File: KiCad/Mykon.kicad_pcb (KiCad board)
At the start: 2 copper layers, 68.4 x 55.4 mm, 27 parts, among them U1 MCP23017_SO, U2 ADS1115IDGS

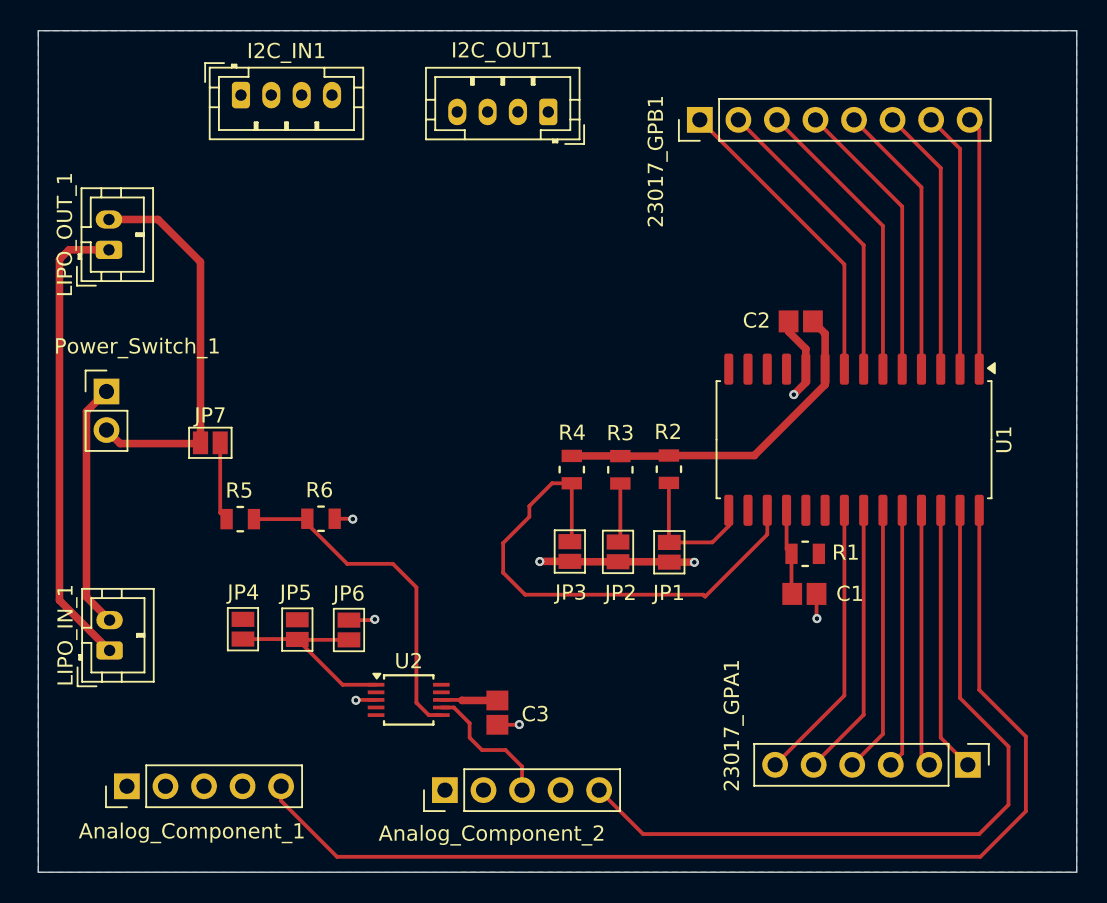
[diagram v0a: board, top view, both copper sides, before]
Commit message: Working ADS1115 and MCP23017
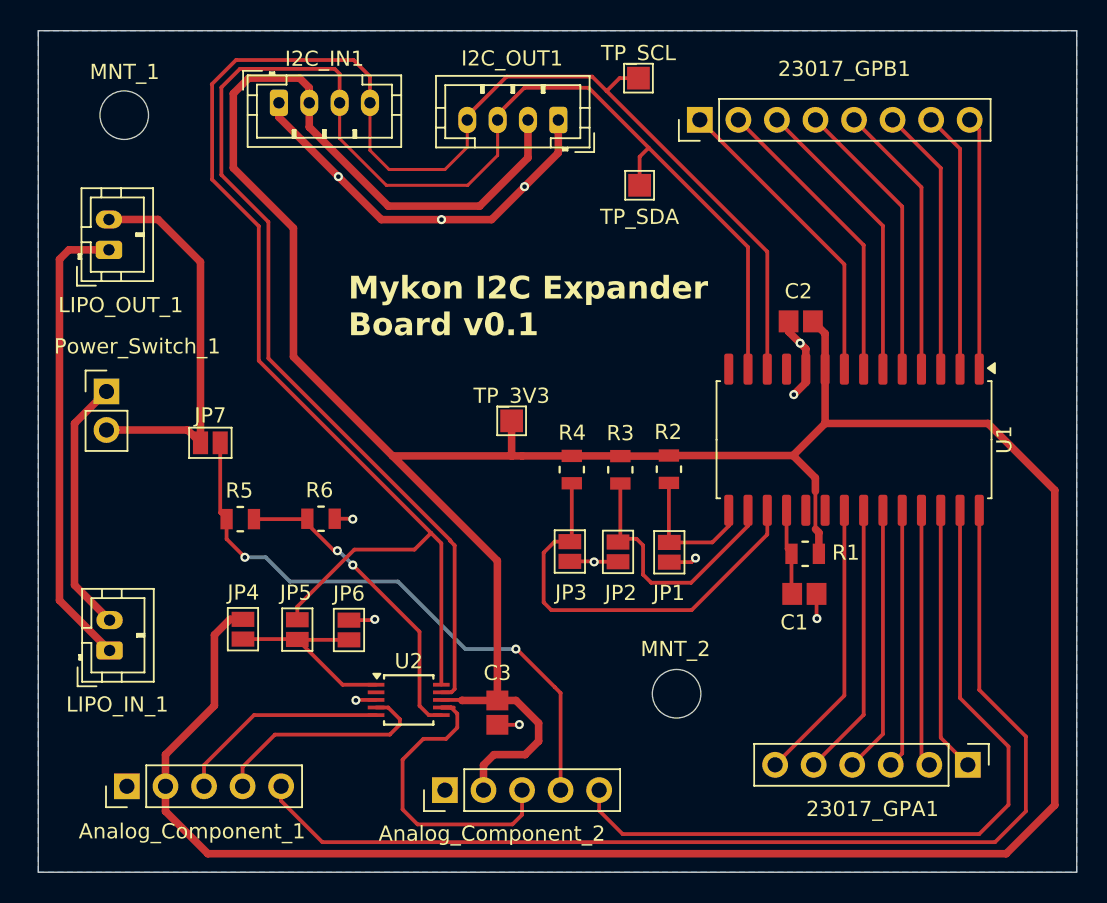
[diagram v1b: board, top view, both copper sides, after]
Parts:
- added MNT_1: MountingHole_3.2mm_M3, MountingHole:MountingHole_3.2mm_M3, F.Cu at (111.9, 77.2)
- added MNT_2: MountingHole_3.2mm_M3, MountingHole:MountingHole_3.2mm_M3, F.Cu at (148.3, 115.3)
- added TP_3V3: TestPoint_Pad_1.5x1.5mm, TestPoint:TestPoint_Pad_1.5x1.5mm, F.Cu at (137.4, 97.3)
- added TP_SCL: TestPoint_Pad_1.5x1.5mm, TestPoint:TestPoint_Pad_1.5x1.5mm, F.Cu at (145.8, 74.8)
- added TP_SDA: TestPoint_Pad_1.5x1.5mm, TestPoint:TestPoint_Pad_1.5x1.5mm, F.Cu at (145.9, 81.8)
- moved I2C_IN1 2.55 mm to (122.1, 76.4)
- moved I2C_OUT1 0.85 mm to (140.5, 77.5)
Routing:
- net +3V3: track 26.9 -> 250.0 mm
- net SCL: track 0.00 -> 119.3 mm
- net SDA: track 0.00 -> 107.2 mm
- net Net-(Analog_Component_2-Pin_4): track 5.20 -> 39.1 mm, vias 0 -> 2
- net GND: track 23.2 -> 44.2 mm, vias 8 -> 12
- net Net-(Analog_Component_1-Pin_4): track 0.00 -> 15.0 mm
- net Net-(Analog_Component_1-Pin_3): track 0.00 -> 14.1 mm
- net Net-(JP2-A): track 3.92 -> 17.0 mm
- net Net-(Analog_Component_2-Pin_3): track 9.04 -> 20.9 mm
- net Net-(JP3-A): track 33.8 -> 27.8 mm
- net Net-(U2-AIN2): track 22.4 -> 20.8 mm, vias 0 -> 2
- net /SW_ANALOG_1: track 73.9 -> 73.1 mm
- net /SW_ANALOG_2: track 49.7 -> 50.5 mm
- net Net-(LIPO_IN_1-Pin_2): track 16.2 -> 16.9 mm
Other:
- board text added: "Mykon I2C Expander Board v0.1"
